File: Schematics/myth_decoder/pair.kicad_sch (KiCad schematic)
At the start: 3 parts, among them U16 74AHC138, U17 74HC238, U18 74AHC138

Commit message: Change d to g
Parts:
- added C1011: C 100nF, Capacitor_THT:C_Disc_D5.0mm_W2.5mm_P2.50mm, symbol Device:C_Small
- added C1012: CP 10μF, Capacitor_THT:CP_Radial_D6.3mm_P2.50mm, symbol Device:C_Polarized_Small
- renumbered U16 to U1016, U17 to U1017, U18 to U1018
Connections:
- net GND: now also C1011.2, C1012.2
- net VCC: now also C1011.1, C1012.1

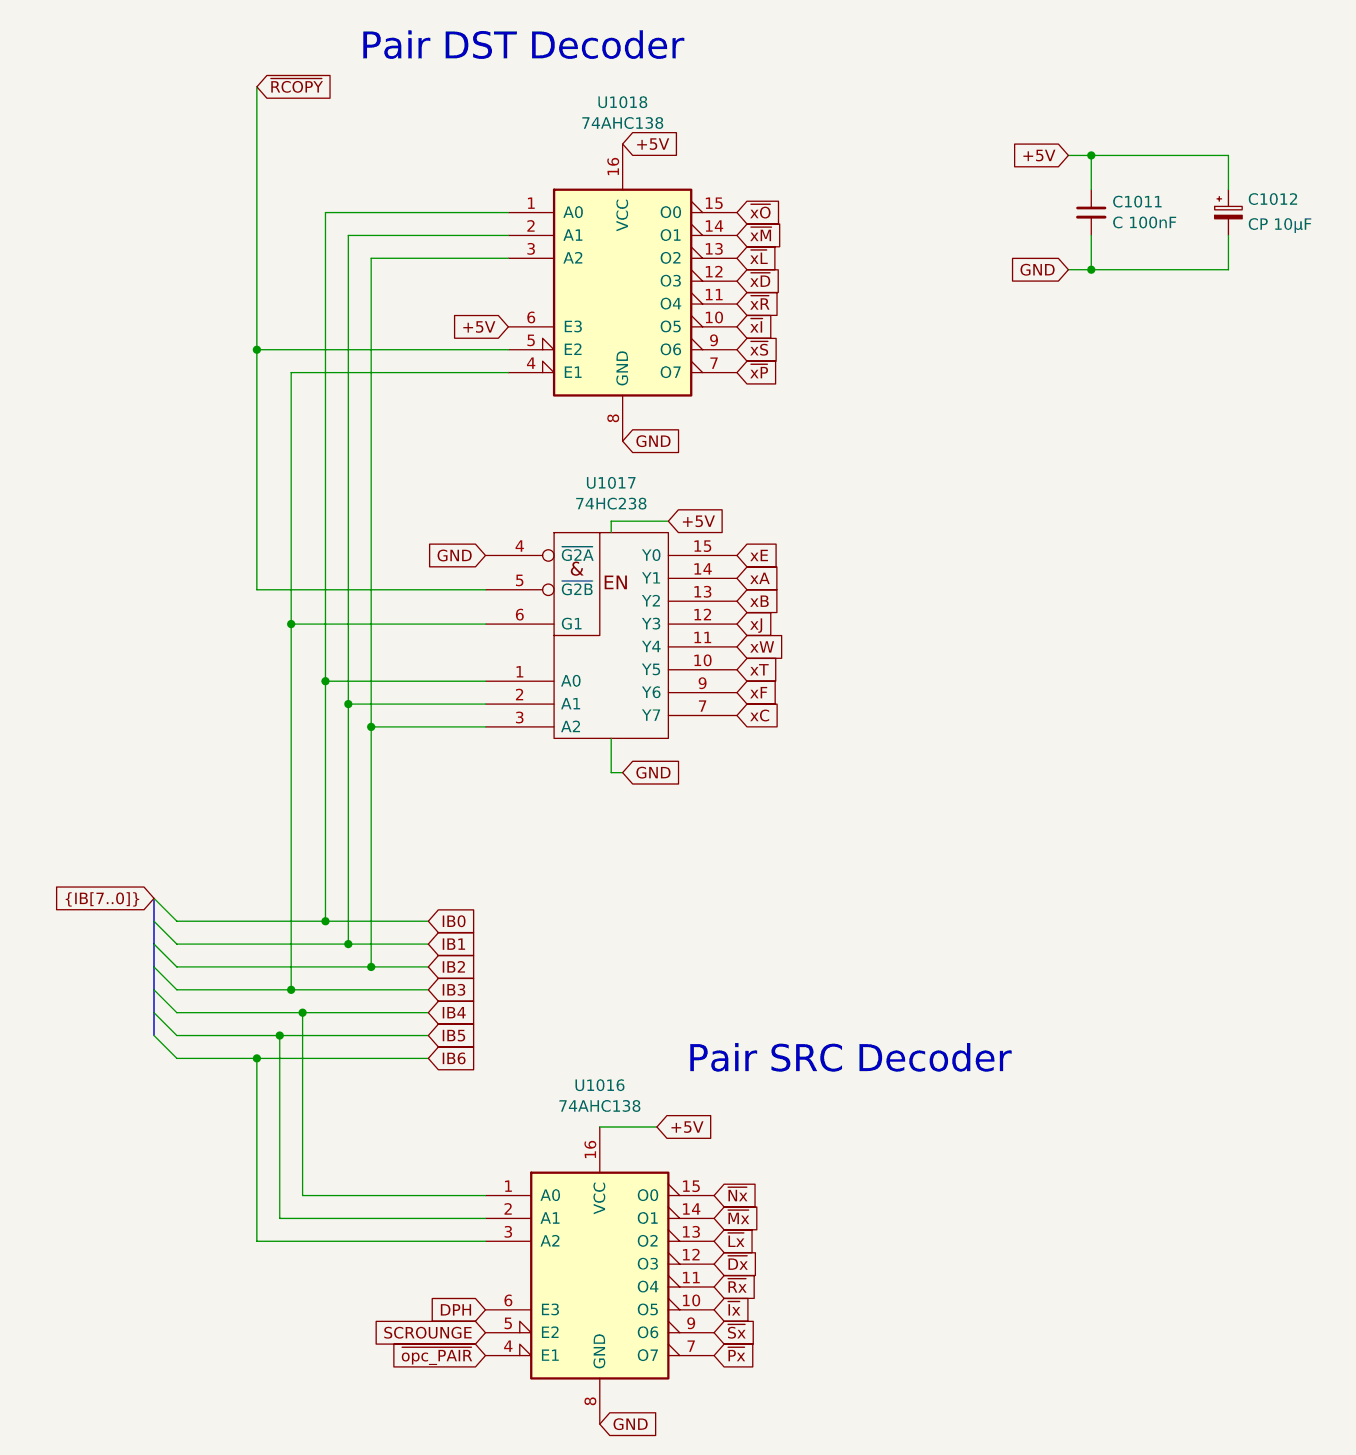
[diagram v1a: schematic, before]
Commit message: Change semantics of xB
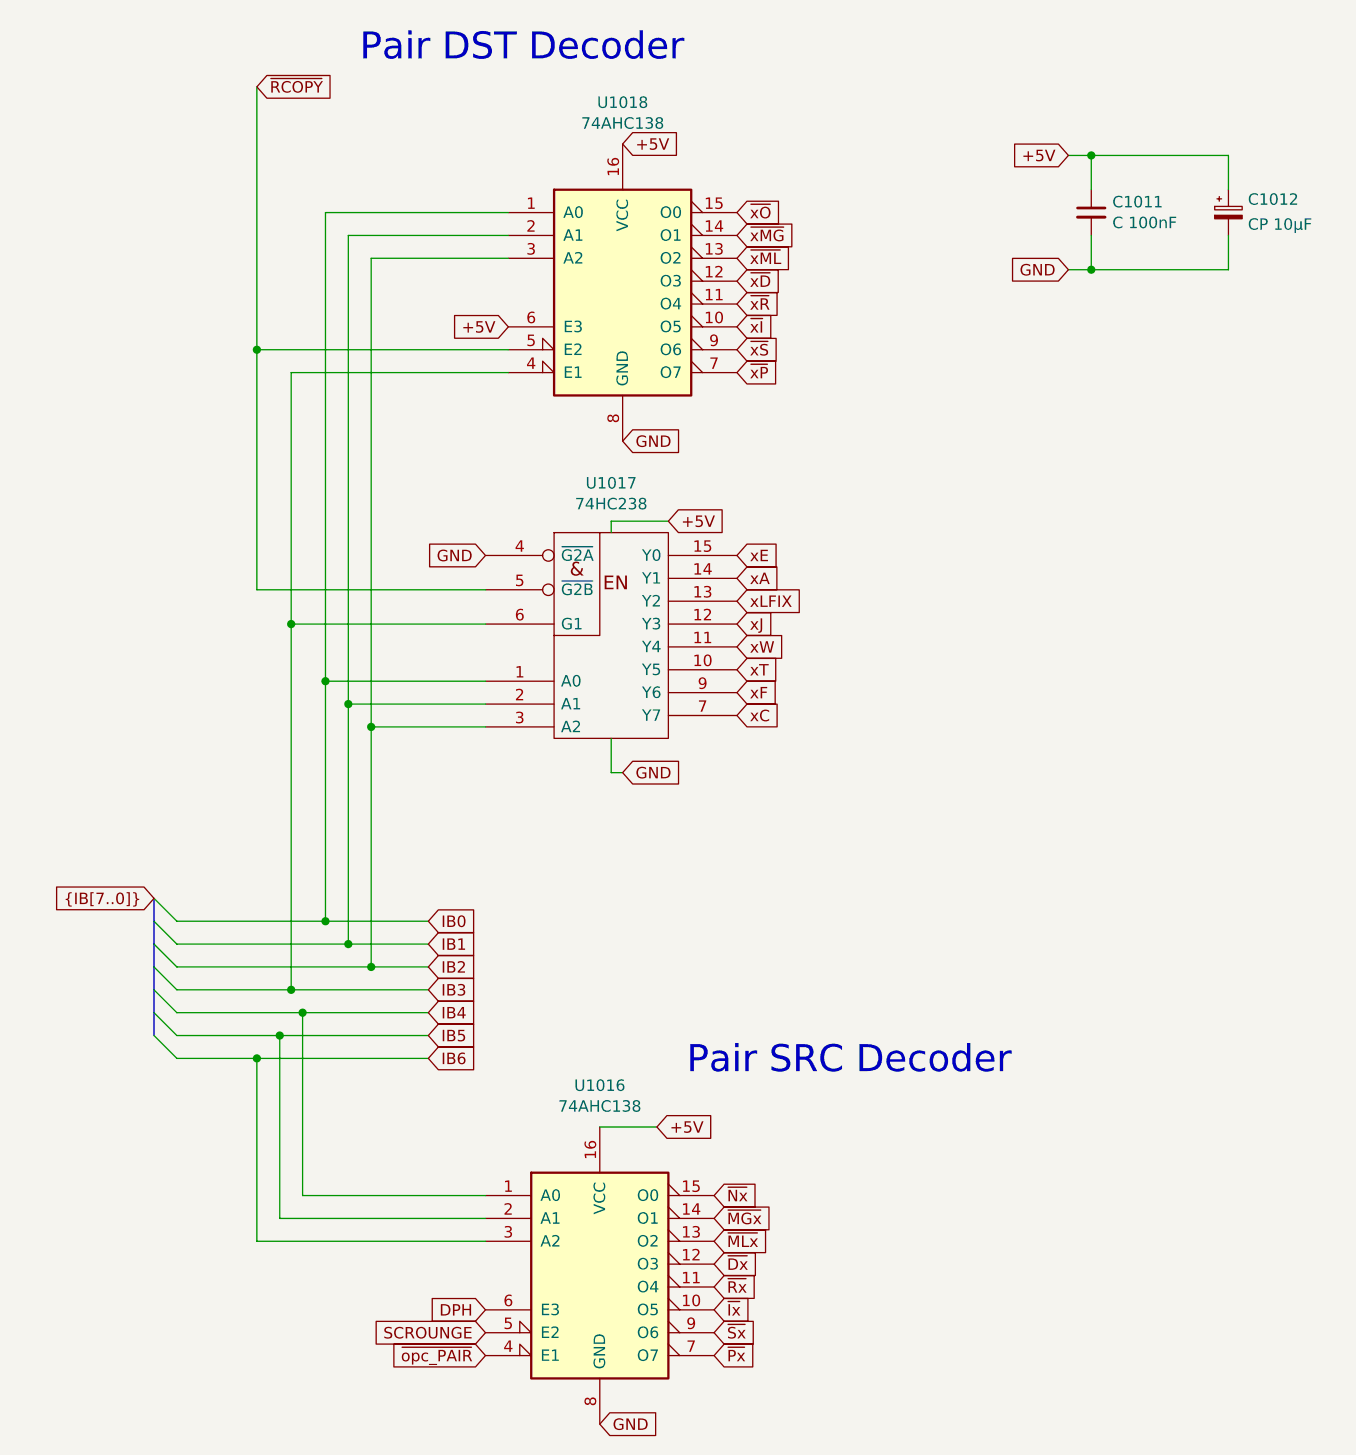
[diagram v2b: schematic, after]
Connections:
- net xB renamed xLFIX
- net ~{Lx} renamed ~{MLx}
- net ~{Mx} renamed ~{MGx}
- net ~{xL} renamed ~{xML}
- net ~{xM} renamed ~{xMG}
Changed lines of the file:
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@@
 		)
 	)
-	(global_label "~{xL}"
+	(global_label "~{xML}"
 		(shape input)
 		(at 134.62 49.53 0)
@@
 		)
 		(property "Intersheetrefs" "${INTERSHEET_REFS}"
-			(at 139.6614 49.53 0)
-			(effects
-				(font
-					(size 1.27 1.27)
-				)
-				(justify left)
-				(hide yes)
-			)
-		)
-	)
-	(global_label "~{xM}"
+			(at 141.1128 49.53 0)
+			(effects
+				(font
+					(size 1.27 1.27)
+				)
+				(justify left)
+				(hide yes)
+			)
+		)
+	)
+	(global_label "~{xMG}"
 		(shape input)
 		(at 134.62 46.99 0)
@@
 		)
 		(property "Intersheetrefs" "${INTERSHEET_REFS}"
-			(at 140.0847 46.99 0)
+			(at 141.3547 46.99 0)
 			(effects
 				(font
@@
 		)
 	)
-	(global_label "~{Mx}"
+	(global_label "~{MGx}"
 		(shape input)
 		(at 132.08 156.21 0)
@@
 		)
 		(property "Intersheetrefs" "${INTERSHEET_REFS}"
-			(at 137.5447 156.21 0)
+			(at 138.8147 156.21 0)
 			(effects
 				(font
@@
 		)
 	)
-	(global_label "~{Lx}"
+	(global_label "~{MLx}"
 		(shape input)
 		(at 132.08 158.75 0)
@@
 		)
 		(property "Intersheetrefs" "${INTERSHEET_REFS}"
-			(at 137.1214 158.75 0)
+			(at 138.5728 158.75 0)
 			(effects
 				(font
@@
 		)
 	)
-	(global_label "xB"
+	(global_label "xLFIX"
 		(shape input)
 		(at 134.62 87.63 0)

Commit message: Change signal names
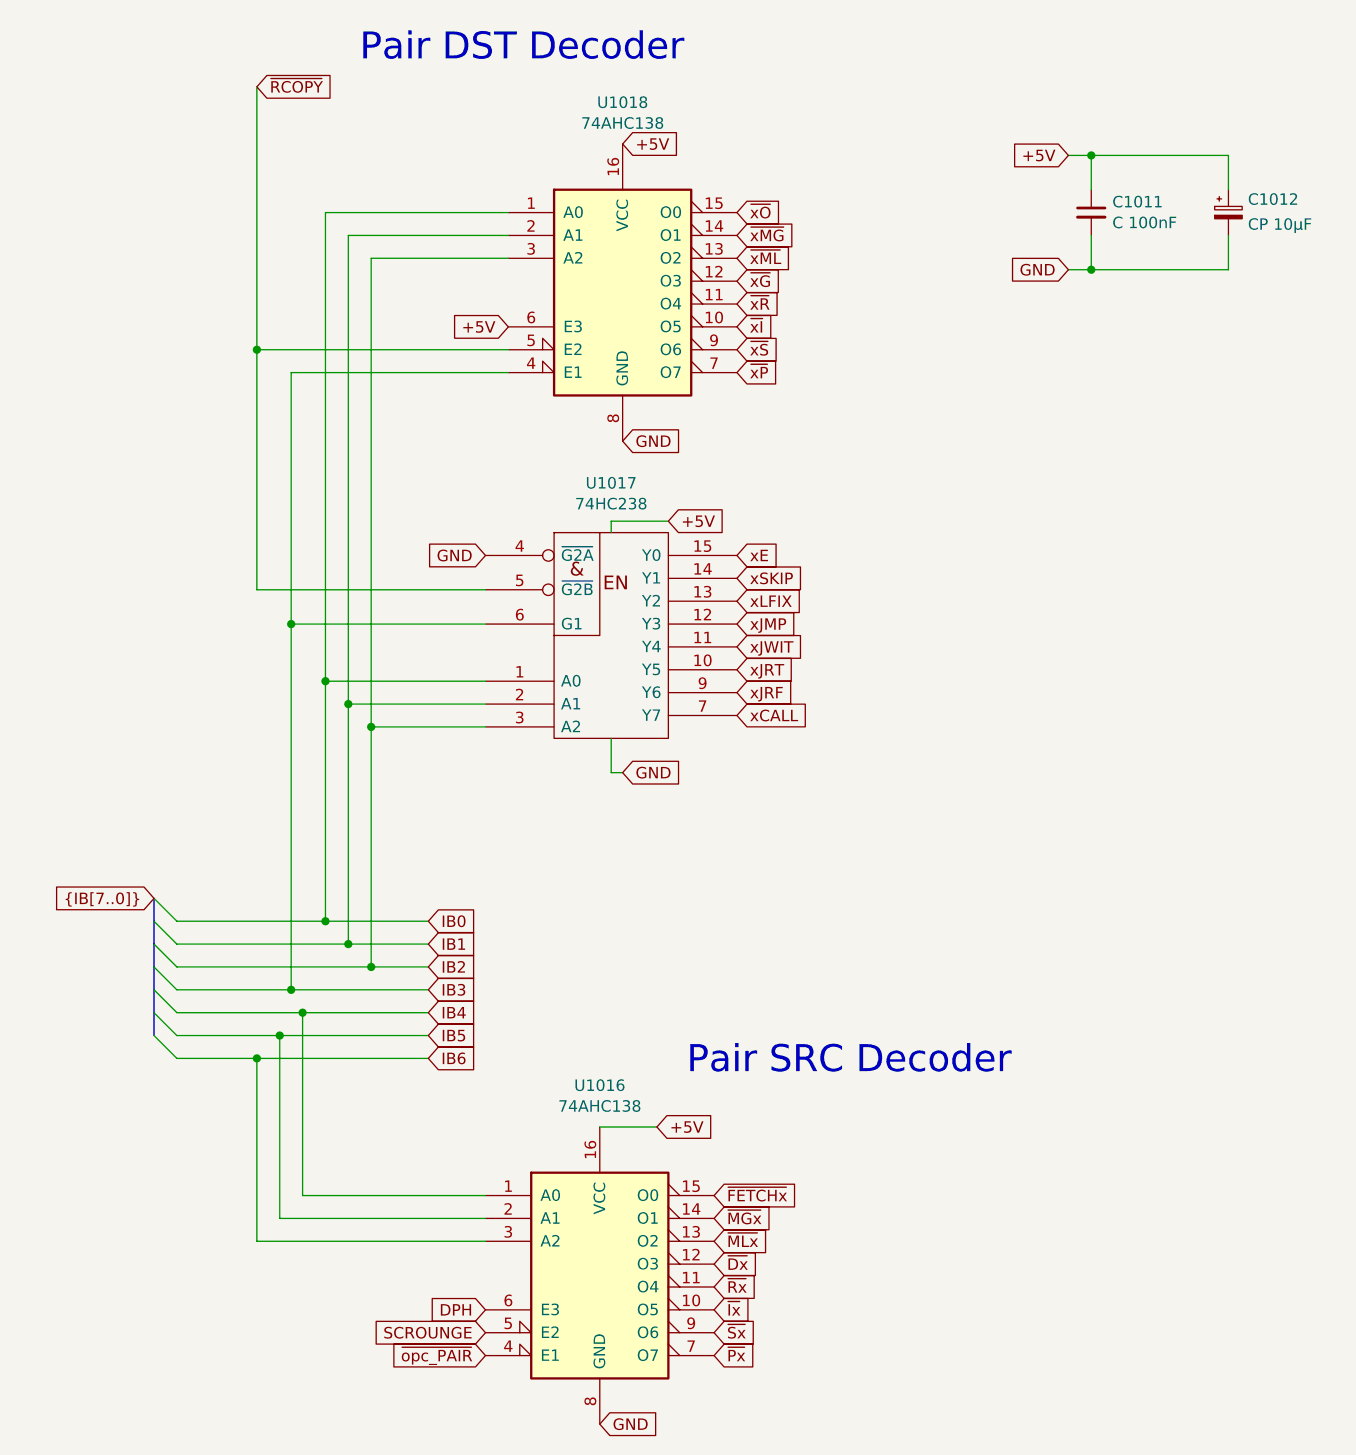
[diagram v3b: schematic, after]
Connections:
- net xA renamed xSKIP
- net xC renamed xCALL
- net xF renamed xJRF
- net xJ renamed xJMP
- net xT renamed xJRT
- net xW renamed xJWIT
- net ~{Nx} renamed ~{FETCHx}
- net ~{xD} renamed ~{xG}
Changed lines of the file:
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@@
 		)
 	)
-	(global_label "~{Nx}"
+	(global_label "~{FETCHx}"
 		(shape input)
 		(at 132.08 153.67 0)
@@
 		)
 	)
-	(global_label "xF"
+	(global_label "xJRF"
 		(shape input)
 		(at 134.62 97.79 0)
@@
 		)
 	)
-	(global_label "xJ"
+	(global_label "xJMP"
 		(shape input)
 		(at 134.62 90.17 0)
@@
 		)
 	)
-	(global_label "xW"
+	(global_label "xJWIT"
 		(shape input)
 		(at 134.62 92.71 0)
@@
 		)
 	)
-	(global_label "~{xD}"
+	(global_label "~{xG}"
 		(shape input)
 		(at 134.62 52.07 0)
@@
 		)
 	)
-	(global_label "xC"
+	(global_label "xCALL"
 		(shape input)
 		(at 134.62 100.33 0)
@@
 		)
 	)
-	(global_label "xA"
+	(global_label "xSKIP"
 		(shape input)
 		(at 134.62 85.09 0)
@@
 		)
 	)
-	(global_label "xT"
+	(global_label "xJRT"
 		(shape input)
 		(at 134.62 95.25 0)
